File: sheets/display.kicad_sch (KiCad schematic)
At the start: 28 parts, among them J10 FH34SRJ-24S-0.5SH_99_E2417KS0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, Q3 Si1308EDL, U14 TXU0104PWR, U15 SN74LXC1T45DCKR, U16 TCK107AF,LF

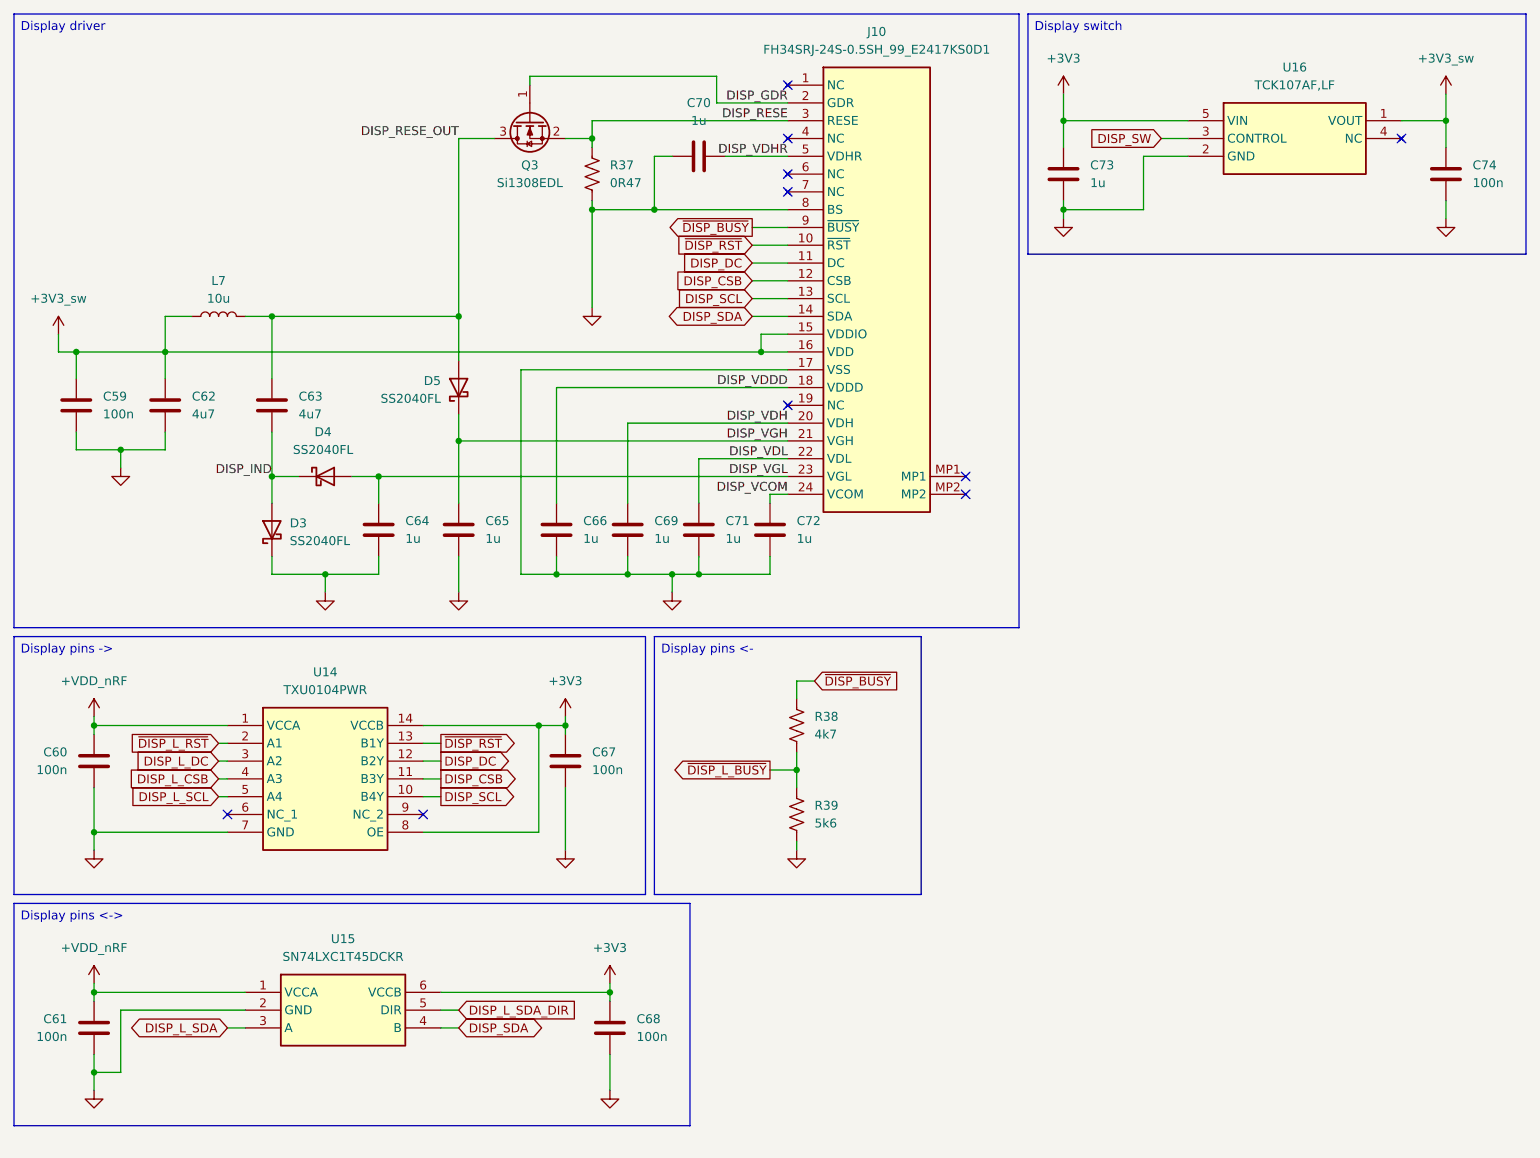
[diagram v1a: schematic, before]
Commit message: Add project symbols and footprints
Move all self-made symbols and footprints to the lib folder.
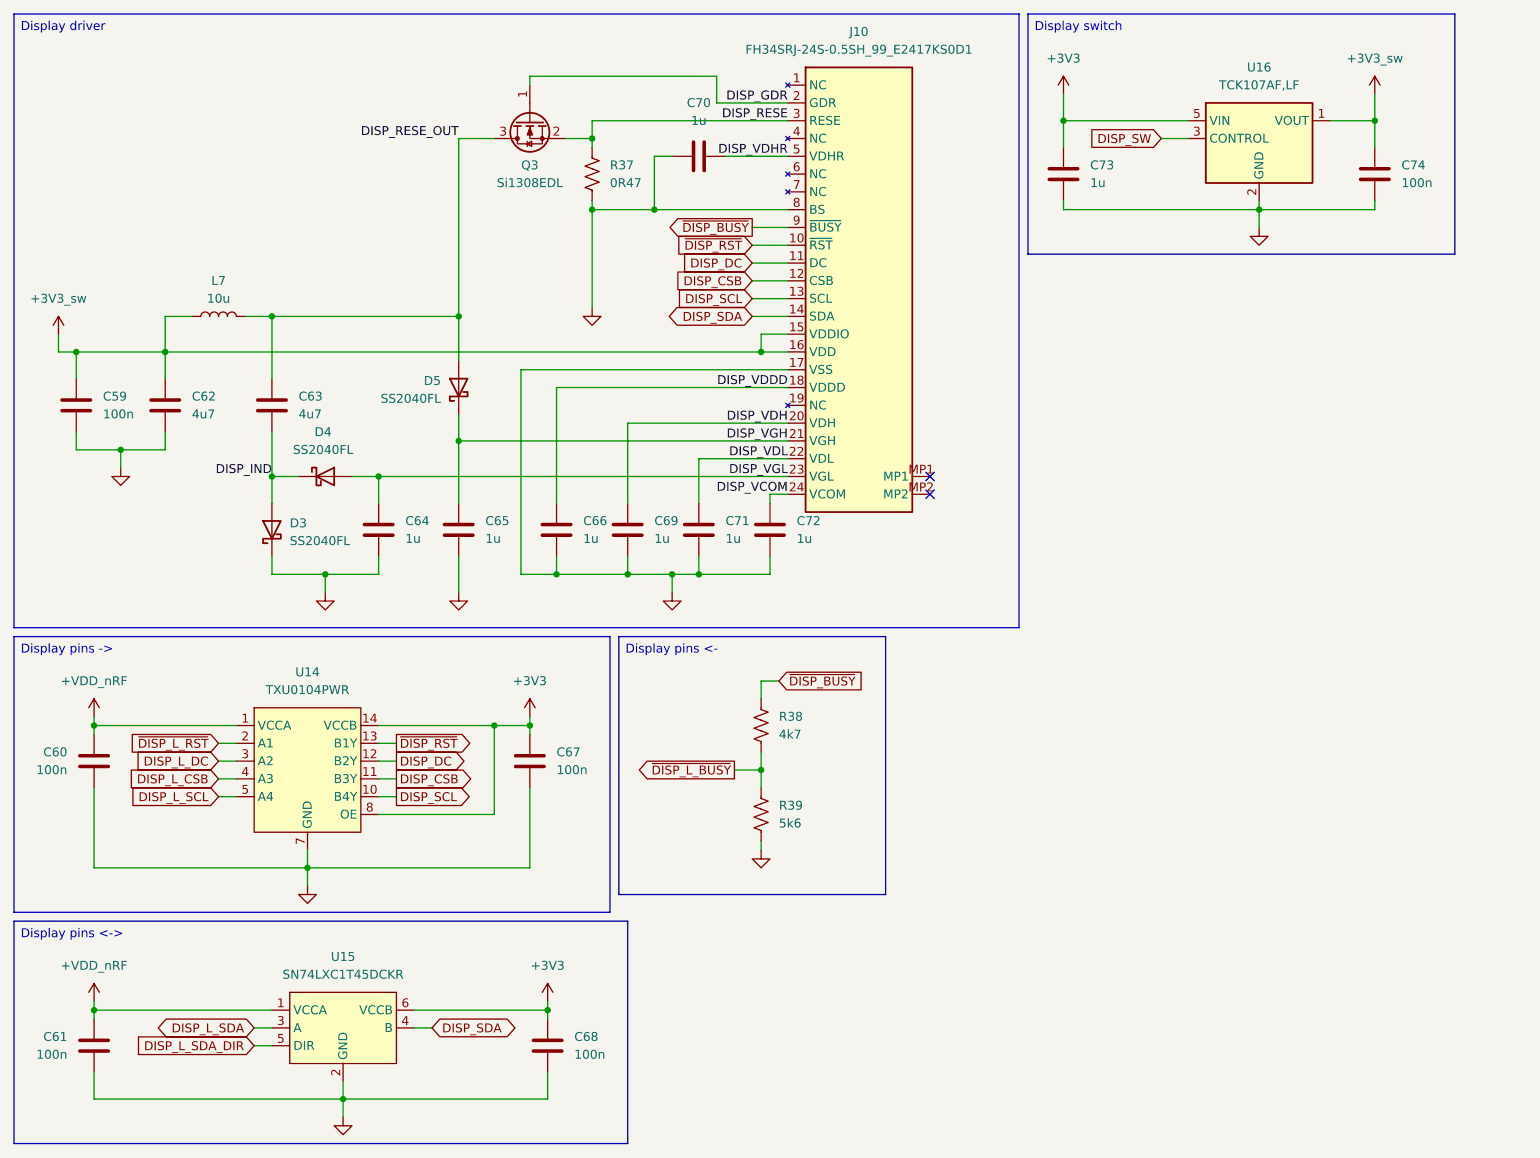
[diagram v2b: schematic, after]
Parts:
- removed U14: TXU0104PWR, TXU0104PWR:SOP65P640X120-14N, symbol TXU0104PWR:TXU0104PWR
- added U14: TXU0104PWR, Package_SO:TSSOP-14_4.4x5mm_P0.65mm, symbol TXU0104:TXU0104
- D3, D4, D5: footprint SS2040FL_R1_00001:SODFL3618X110N -> Diode_SMD:D_SOD-123F
- J10: symbol FH34SRJ-24S-0.5SH_99_E2417KS0D1:FH34SRJ-24S-0.5SH_99_ -> Connector_Display:FH34SRJ-24S-0.5SH
- U15: footprint SN74LXC1T45DCKR:SOT65P210X110-6N -> Package_TO_SOT_SMD:SOT-363_SC-70-6; symbol SN74LXC1T45DCKR:SN74LXC1T45DCKR -> SN74LXC1T45:SN74LXC1T45DCK
- U16: symbol TCK107AF_LF:TCK107AF,LF -> TCK10xAF:TCK107AF
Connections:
- net +3V3: now also U14.14 (VCCB), U14.8 (OE)
- net +VDD_nRF: now also U14.1 (VCCA)
- net DISP_CSB: now also U14.11 (B3Y)
- net DISP_DC: now also U14.12 (B2Y)
- net DISP_L_CSB: now also U14.4 (A3)
- net DISP_L_DC: now also U14.3 (A2)
- net DISP_L_SCL: now also U14.5 (A4)
- net DISP_SCL: now also U14.10 (B4Y)
- net GND: now also U14.7 (GND)
- net ~{DISP_L_RST}: now also U14.2 (A1)
- net ~{DISP_RST}: now also U14.13 (B1Y)
- new net: U14.6 (NC), U14.9 (NC)
- no-connect marks 10 -> 2
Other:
- moved on the sheet: C61, C67, C68, C74, J10, R38, R39, U15
